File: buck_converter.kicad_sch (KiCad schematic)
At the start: 46 parts, among them U3 LMR604403SRAKR, U4 LMR604403SRAKR

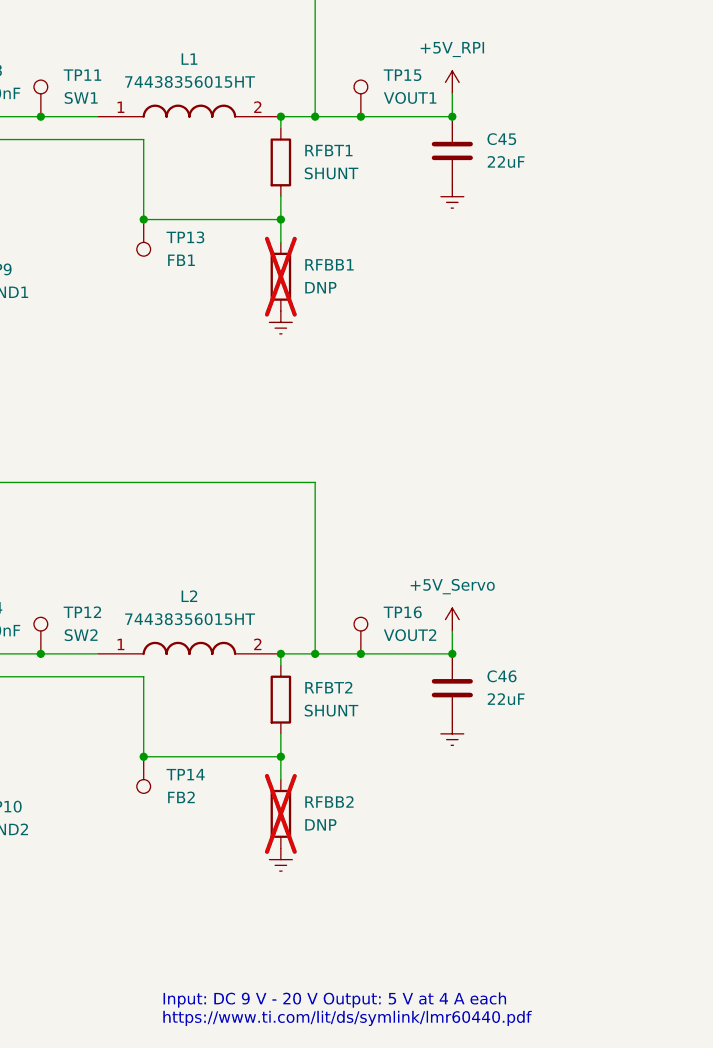
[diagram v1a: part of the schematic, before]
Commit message: correct feedback resistors on buck converters
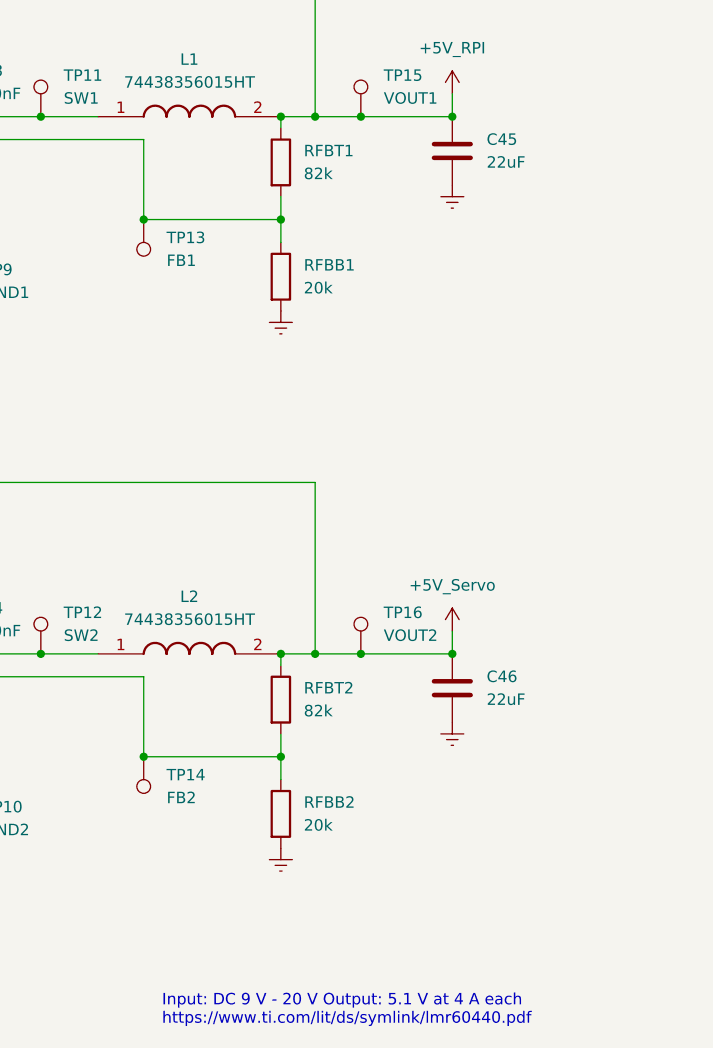
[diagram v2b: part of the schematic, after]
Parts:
- RFBB1, RFBB2: value DNP -> 20k; now fitted
- RFBT1, RFBT2: value SHUNT -> 82k
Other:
- note added: "Input: DC 9 V - 20 V Output: 5.1 V at 4 A each https://www.ti.com/lit/ds/symlink/lmr60440.pdf"
- note removed: "Input: DC 9 V - 20 V Output: 5 V at 4 A each https://www.ti.com/lit/ds/symlink/lmr60440.pdf"
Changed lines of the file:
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@@
 	(title_block
 		(title "RSC hat board")
-		(date "2026-05-18")
+		(date "2026-05-19")
 		(rev "A")
 		(comment 1 "Author: Raiko Torga")
 	)
-	(text "Input: DC 9 V - 20 V Output: 5 V at 4 A each\nhttps://www.ti.com/lit/ds/symlink/lmr60440.pdf"
+	(text "Input: DC 9 V - 20 V Output: 5.1 V at 4 A each\nhttps://www.ti.com/lit/ds/symlink/lmr60440.pdf"
 		(exclude_from_sim no)
 		(at 178.562 169.164 0)
@@
 			)
 		)
-		(property "Value" "SHUNT"
+		(property "Value" "82k"
 			(at 194.31 76.1999 0)
 			(effects
@@
 		(in_bom yes)
 		(on_board yes)
-		(dnp yes)
+		(dnp no)
 		(fields_autoplaced yes)
 		(property "Reference" "RFBB2"
@@
 			)
 		)
-		(property "Value" "DNP"
+		(property "Value" "20k"
 			(at 194.31 148.5899 0)
 			(effects
@@
 			)
 		)
-		(property "Value" "SHUNT"
+		(property "Value" "82k"
 			(at 194.31 135.8899 0)
 			(effects
@@
 		(in_bom yes)
 		(on_board yes)
-		(dnp yes)
+		(dnp no)
 		(fields_autoplaced yes)
 		(property "Reference" "RFBB1"
@@
 			)
 		)
-		(property "Value" "DNP"
+		(property "Value" "20k"
 			(at 194.31 88.8999 0)
 			(effects
